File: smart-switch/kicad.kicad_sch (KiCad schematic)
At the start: 12 parts

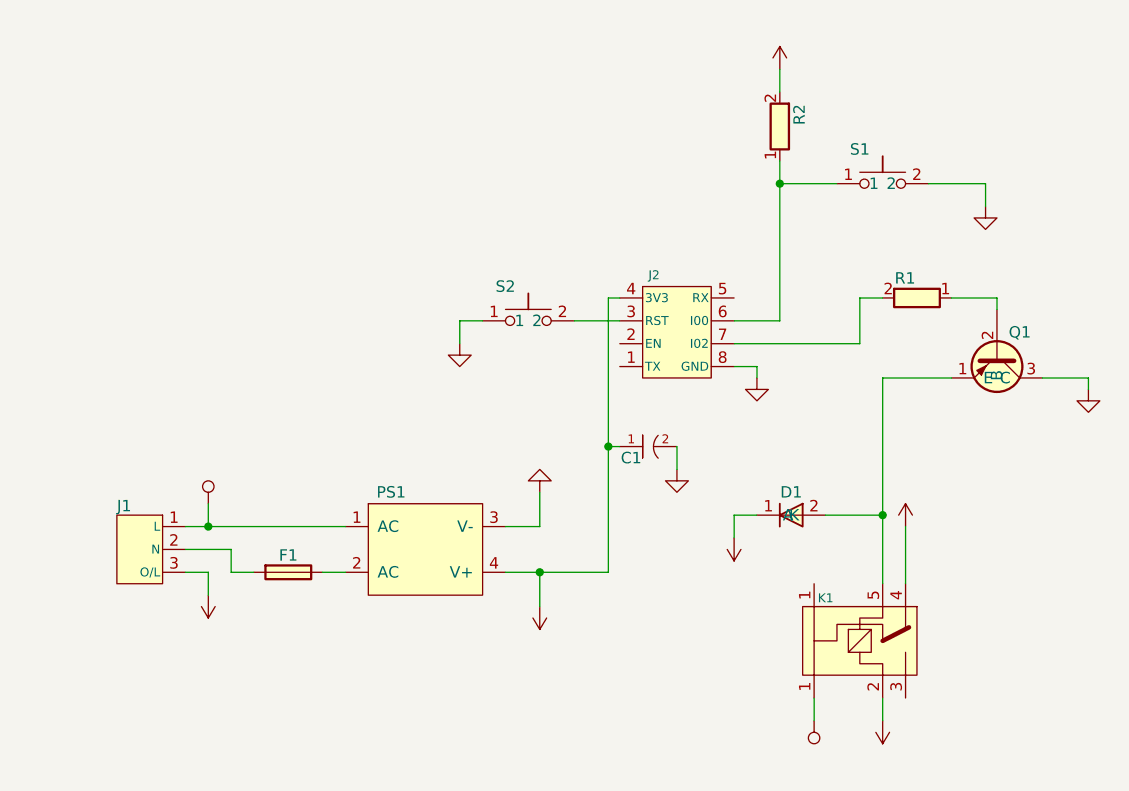
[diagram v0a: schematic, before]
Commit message: Update smart switch 3d model
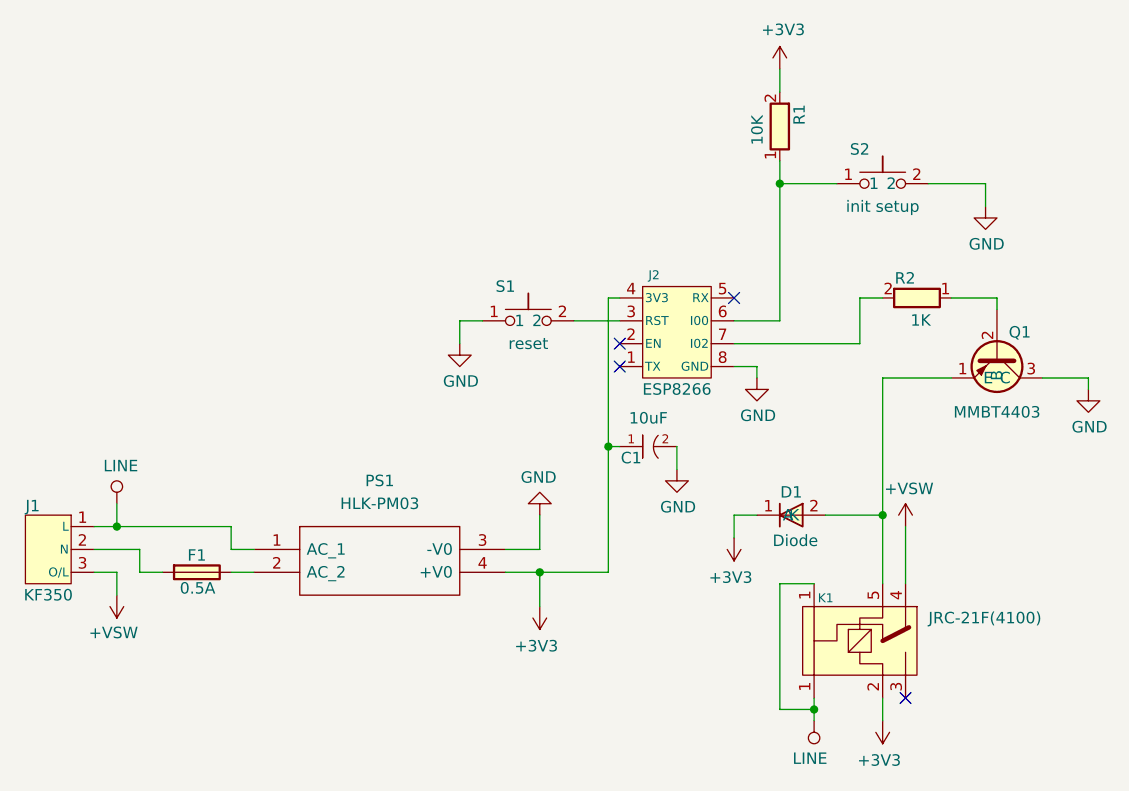
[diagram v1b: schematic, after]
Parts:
- removed PS1: (no value), symbol kicad-rescue:HLK-PM-local
- added PS1: HLK-PM03, HLK-PM03:HLKPM03, symbol HLK-PM03:HLK-PM03
- C1: value (none) -> 10uF; footprint (none) -> footprints:C_1206_3216Metric
- D1: value (none) -> Diode; footprint (none) -> footprints:D_SMA
- F1: value (none) -> 0.5A; footprint (none) -> footprints:Fuse
- J1: value (none) -> KF350; footprint (none) -> footprints:KF350
- J2: value (none) -> ESP8266; footprint (none) -> footprints:ESP8266
- K1: value (none) -> JRC-21F(4100); footprint (none) -> footprints:JRC-21F(4100)
- Q1: value (none) -> MMBT4403; footprint (none) -> footprints:SOT-23
- R1: renamed from R2; value (none) -> 10K; footprint (none) -> footprints:R_0805_2012Metric
- R2: renamed from R1; value (none) -> 1K; footprint (none) -> footprints:R_0805_2012Metric
- S1: renamed from S2; value (none) -> reset; footprint (none) -> footprints:SW_Tactile
- S2: renamed from S1; value (none) -> init setup; footprint (none) -> footprints:SW_Tactile
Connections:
- net +3V3: now also PS1.4 (+V0)
- net GND: now also PS1.3 (-V0)
- net LINE: now also PS1.1 (AC_1)
- net at F1.1: now also PS1.2 (AC_2)
- no-connect marks 0 -> 4
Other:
- moved on the sheet: F1, J1
